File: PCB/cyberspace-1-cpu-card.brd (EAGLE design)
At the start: 100 x 50 mm, 26 parts, among them J1 Connector, 6P, SM, VT, J2 Connector, 6P, SM, VT, J3 Connector, 6P, SM, VT, J4 HEADER, FEMALE, 10P, U1 6502 Processor, U2 16V8, U3 16V8, U4 W65C22

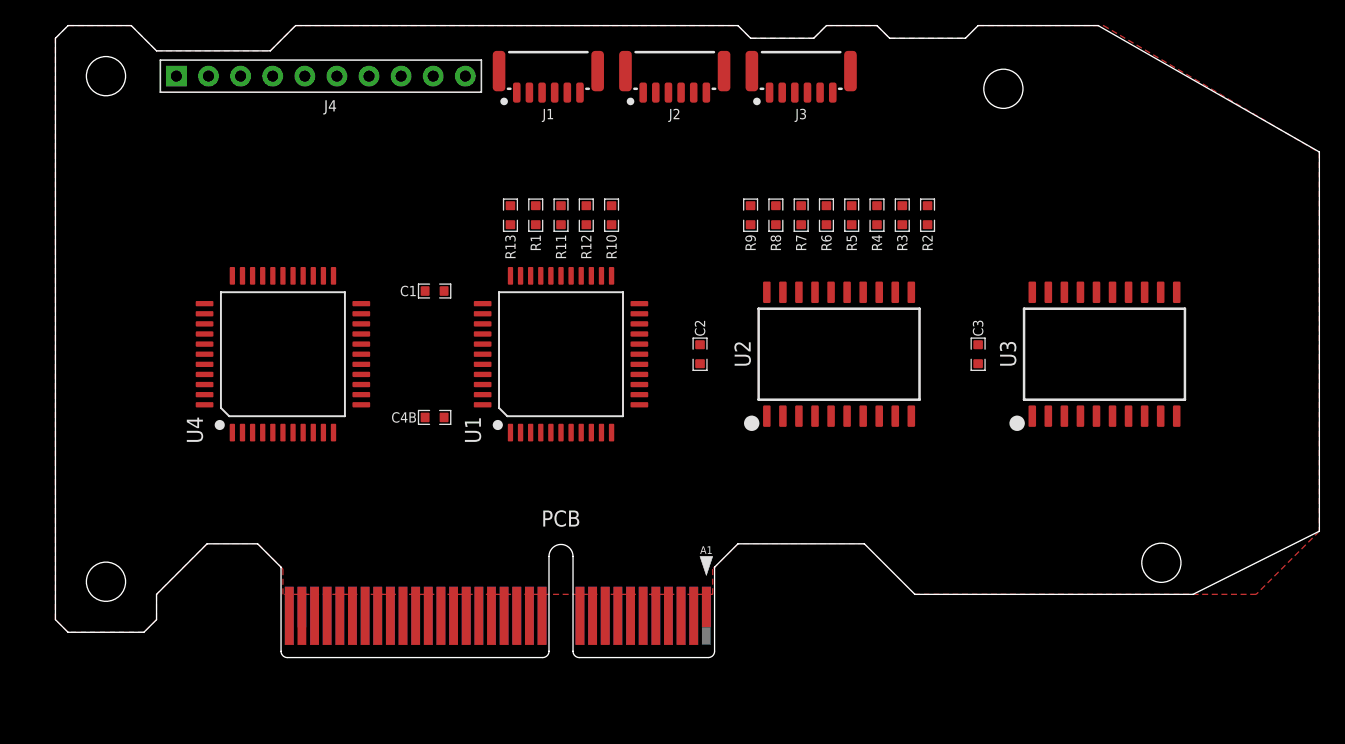
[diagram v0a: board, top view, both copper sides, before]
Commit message: CPU PCB routed.
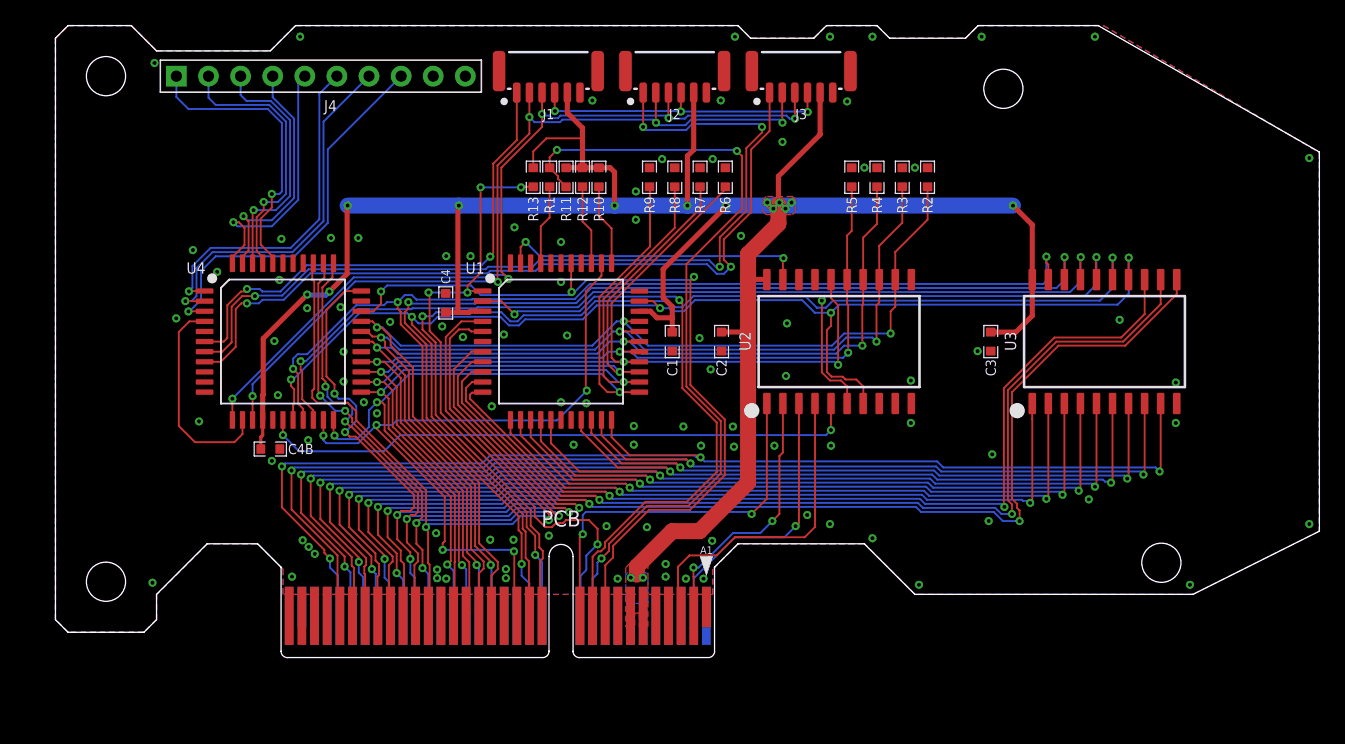
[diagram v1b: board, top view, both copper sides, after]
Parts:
- added C4: 0.1uF, rlc:0603-CAP
- moved C1 19.2 mm to (48.8, 25.0), turned to 270 degrees
- moved C4B 13.2 mm to (17.0, 16.5), turned to 0 degrees
- moved R6 8.54 mm to (53.0, 38.0)
- moved R7 8.54 mm to (51.0, 38.0)
- moved R8 8.54 mm to (49.0, 38.0)
- moved R9 8.54 mm to (47.0, 38.0)
- moved R13 3.50 mm to (37.8, 38.0)
- moved R1 3.20 mm to (39.1, 38.0)
- moved R10 3.16 mm to (43.0, 38.0)
- moved R11 3.03 mm to (40.4, 38.0)
- moved R12 3.01 mm to (41.7, 38.0)
- moved R2 3.00 mm to (69.0, 38.0)
- moved R3 3.00 mm to (67.0, 38.0)
- moved R4 3.00 mm to (65.0, 38.0)
- moved R5 3.00 mm to (63.0, 38.0)
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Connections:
- removed net RES1: U2.2
- removed net RES2: U2.3
- removed net RES3: U2.4
- new net !INT2: PCB.A2, U2.2
- new net !INT3: PCB.B2, U2.3
- new net !INT4: PCB.A3, U2.4
- net GND: now also C4.2
- net VCC: now also C4.1
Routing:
- net VCC: track 0.00 -> 195.6 mm, vias 0 -> 15
- net !W: track 0.00 -> 118.8 mm, vias 0 -> 6
- net A4: track 0.00 -> 104.8 mm, vias 0 -> 3
- net A5: track 0.00 -> 103.7 mm, vias 0 -> 4
- net A6: track 0.00 -> 102.4 mm, vias 0 -> 3
- net !IORQ: track 0.00 -> 100.6 mm, vias 0 -> 4
- net A15: track 0.00 -> 98.5 mm, vias 0 -> 4
- net A14: track 0.00 -> 96.1 mm, vias 0 -> 3
- net A13: track 0.00 -> 94.3 mm, vias 0 -> 4
- net A11: track 0.00 -> 92.3 mm, vias 0 -> 4
- net A12: track 0.00 -> 92.1 mm, vias 0 -> 3
- net A10: track 0.00 -> 90.1 mm, vias 0 -> 3
- net !R: track 0.00 -> 89.2 mm, vias 0 -> 2
- net A9: track 0.00 -> 88.1 mm, vias 0 -> 4
- net D4: track 0.00 -> 87.0 mm, vias 0 -> 3
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- added copper zone on layer 16, net GND
- added copper zone on layer 1, net VCC
- added copper zone on layer 16, net VCC

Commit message: GitHub did something weird. All new files and no idea why.
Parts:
- removed C4B: 0.1uF, rlc:0603-CAP
- added C1B: 0.1uF, rlc:0603-CAP
- added LED1, LED2, LED3, LED4: BLU, led:SMD_0603
- added R14, R15, R16, R17: 470, rlc:0603-RES
- added U$2: NO-FERMIUM-5MM, gfx-glyphs:NO-FERMIUM-5MM
- moved C4 18.1 mm to (17.0, 16.5), turned to 0 degrees
- renumbered C1 to C1A
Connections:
- new net N$11: LED1.A, R14.1
- new net N$12: LED2.A, R15.1
- new net N$13: LED3.A, R16.1
- new net N$14: LED4.A, R17.1
- net !IRQ: now also PCB.A4
- net BE: now also PCB.B3
- net GND: now also C1B.2, LED1.K, LED2.K, LED3.K, LED4.K; no longer C4B.2
- net VCC: now also C1B.1, R14.2, R15.2, R16.2, R17.2; no longer C4B.1
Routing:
- net VCC: track 195.6 -> 216.6 mm
- net N$14: track 0.00 -> 4.19 mm, vias 0 -> 1
- net N$13: track 0.00 -> 3.50 mm, vias 0 -> 1
- net N$11: track 0.00 -> 3.24 mm, vias 0 -> 1
- net N$12: track 0.00 -> 3.24 mm, vias 0 -> 1
- net A1: track 65.0 -> 63.6 mm
- net A0: track 64.9 -> 65.7 mm
- net N$5: track 20.4 -> 19.7 mm
- net N$4: track 19.3 -> 18.7 mm
- net A6: track 102.4 -> 101.9 mm
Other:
- board text added: "5000"
- board text added: "Ahti"
- board text added: "CORP"
- board text added: "Cerebrum"
- board text added: "For use in CyberSpace-1 system only!"
- board text added: "GLX"
- board text added: "GLX5000"
- board text added: "Instruction Processor"
- board text added: "Now with 16-bit Mackerel bus!"
- board text added: "P O W E R E D"
- board text added: "TM"
- board text added: "WARNING:"
